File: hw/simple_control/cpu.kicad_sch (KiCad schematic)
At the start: 12 parts, among them J601 Conn_01x04, J602 Raspberry_Pi_0_2_3, J603 Conn_01x03, SW601 SW_Push, U601 PicoW

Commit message: chore(hw): assign footprints
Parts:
- C601, C602, C603: footprint (none) -> Capacitor_SMD:C_0805_2012Metric_Pad1.18x1.45mm_HandSolder
- J602: footprint (none) -> my:Raspberry_Pi_Zero_Socketed_THT_FaceDown_MountingHoles_No_Courtyard
- J603: footprint (none) -> Connector_PinHeader_2.54mm:PinHeader_1x03_P2.54mm_Vertical
- JP601, JP602: footprint (none) -> Jumper:SolderJumper-3_P1.3mm_Bridged12_RoundedPad1.0x1.5mm_NumberLabels
- SW601: footprint (none) -> Button_Switch_THT:SW_PUSH_6mm
- U601: footprint RPi_PicoW:RPi_Pico_SMD_TH -> rp-pico:RPi_PicoW_SMD_TH
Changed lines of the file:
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@@
       (effects (font (size 1.27 1.27)) (justify left))
     )
-    (property "Footprint" "" (at 162.2552 184.15 0)
+    (property "Footprint" "Capacitor_SMD:C_0805_2012Metric_Pad1.18x1.45mm_HandSolder" (at 162.2552 184.15 0)
       (effects (font (size 1.27 1.27)) hide)
     )
@@
       (effects (font (size 1.27 1.27)) (justify left))
     )
-    (property "Footprint" "" (at 81.28 138.43 0)
+    (property "Footprint" "Connector_PinHeader_2.54mm:PinHeader_1x03_P2.54mm_Vertical" (at 81.28 138.43 0)
       (effects (font (size 1.27 1.27)) hide)
     )
@@
   (symbol (lib_id "power:GND") (at 135.89 187.96 0) (unit 1)
     (in_bom yes) (on_board yes) (dnp no) (fields_autoplaced)
-    (property "Reference" "#PWR0618" (at 135.89 194.31 0)
+    (property "Reference" "#PWR0619" (at 135.89 194.31 0)
       (effects (font (size 1.27 1.27)) hide)
     )
@@
       (project "simple_control"
         (path "/063164e8-0d2a-492b-8a61-e4fa4fbf06a6/3d4e7106-28aa-4335-9fa1-cc7761972854"
-          (reference "#PWR0618") (unit 1)
+          (reference "#PWR0619") (unit 1)
         )
       )
@@
       (effects (font (size 1.27 1.27)) (justify left))
     )
-    (property "Footprint" "" (at 136.8552 184.15 0)
+    (property "Footprint" "Capacitor_SMD:C_0805_2012Metric_Pad1.18x1.45mm_HandSolder" (at 136.8552 184.15 0)
       (effects (font (size 1.27 1.27)) hide)
     )
@@
       (effects (font (size 1.27 1.27)))
     )
-    (property "Footprint" "" (at 259.08 154.94 0)
+    (property "Footprint" "Jumper:SolderJumper-3_P1.3mm_Bridged12_RoundedPad1.0x1.5mm_NumberLabels" (at 259.08 154.94 0)
       (effects (font (size 1.27 1.27)) hide)
     )
@@
       (effects (font (size 1.27 1.27)))
     )
-    (property "Footprint" "" (at 259.08 142.24 0)
+    (property "Footprint" "Jumper:SolderJumper-3_P1.3mm_Bridged12_RoundedPad1.0x1.5mm_NumberLabels" (at 259.08 142.24 0)
       (effects (font (size 1.27 1.27)) hide)
     )
@@
       (effects (font (size 1.27 1.27)) (justify left))
     )
-    (property "Footprint" "" (at 149.5552 184.15 0)
+    (property "Footprint" "Capacitor_SMD:C_0805_2012Metric_Pad1.18x1.45mm_HandSolder" (at 149.5552 184.15 0)
       (effects (font (size 1.27 1.27)) hide)
     )
@@
   (symbol (lib_id "power:GND") (at 88.9 132.08 0) (unit 1)
     (in_bom yes) (on_board yes) (dnp no) (fields_autoplaced)
-    (property "Reference" "#PWR0619" (at 88.9 138.43 0)
+    (property "Reference" "#PWR0617" (at 88.9 138.43 0)
       (effects (font (size 1.27 1.27)) hide)
     )
@@
       (project "simple_control"
         (path "/063164e8-0d2a-492b-8a61-e4fa4fbf06a6/3d4e7106-28aa-4335-9fa1-cc7761972854"
-          (reference "#PWR0619") (unit 1)
+          (reference "#PWR0617") (unit 1)
         )
       )
@@
   (symbol (lib_id "power:+5V") (at 135.89 172.72 0) (unit 1)
     (in_bom yes) (on_board yes) (dnp no) (fields_autoplaced)
-    (property "Reference" "#PWR0617" (at 135.89 176.53 0)
+    (property "Reference" "#PWR0618" (at 135.89 176.53 0)
       (effects (font (size 1.27 1.27)) hide)
     )
@@
       (project "simple_control"
         (path "/063164e8-0d2a-492b-8a61-e4fa4fbf06a6/3d4e7106-28aa-4335-9fa1-cc7761972854"
-          (reference "#PWR0617") (unit 1)
+          (reference "#PWR0618") (unit 1)
         )
       )
@@
       (effects (font (size 1.27 1.27)))
     )
-    (property "Footprint" "RPi_PicoW:RPi_Pico_SMD_TH" (at 81.28 99.06 90)
+    (property "Footprint" "rp-pico:RPi_PicoW_SMD_TH" (at 81.28 99.06 90)
       (effects (font (size 1.27 1.27)) hide)
     )
@@
       (effects (font (size 1.27 1.27)) (justify left))
     )
-    (property "Footprint" "" (at 165.1 102.87 0)
+    (property "Footprint" "Button_Switch_THT:SW_PUSH_6mm" (at 165.1 102.87 0)
       (effects (font (size 1.27 1.27)) hide)
     )
@@
       (effects (font (size 1.27 1.27)) (justify left))
     )
-    (property "Footprint" "" (at 218.44 62.23 0)
-      (effects (font (size 1.27 1.27)) hide)
-    )
+    (property "Footprint" "my:Raspberry_Pi_Zero_Socketed_THT_FaceDown_MountingHoles_No_Courtyard" (at 218.44 62.23 0)
+      (effects (font (size 1.27 1.27)) hide)
+    )

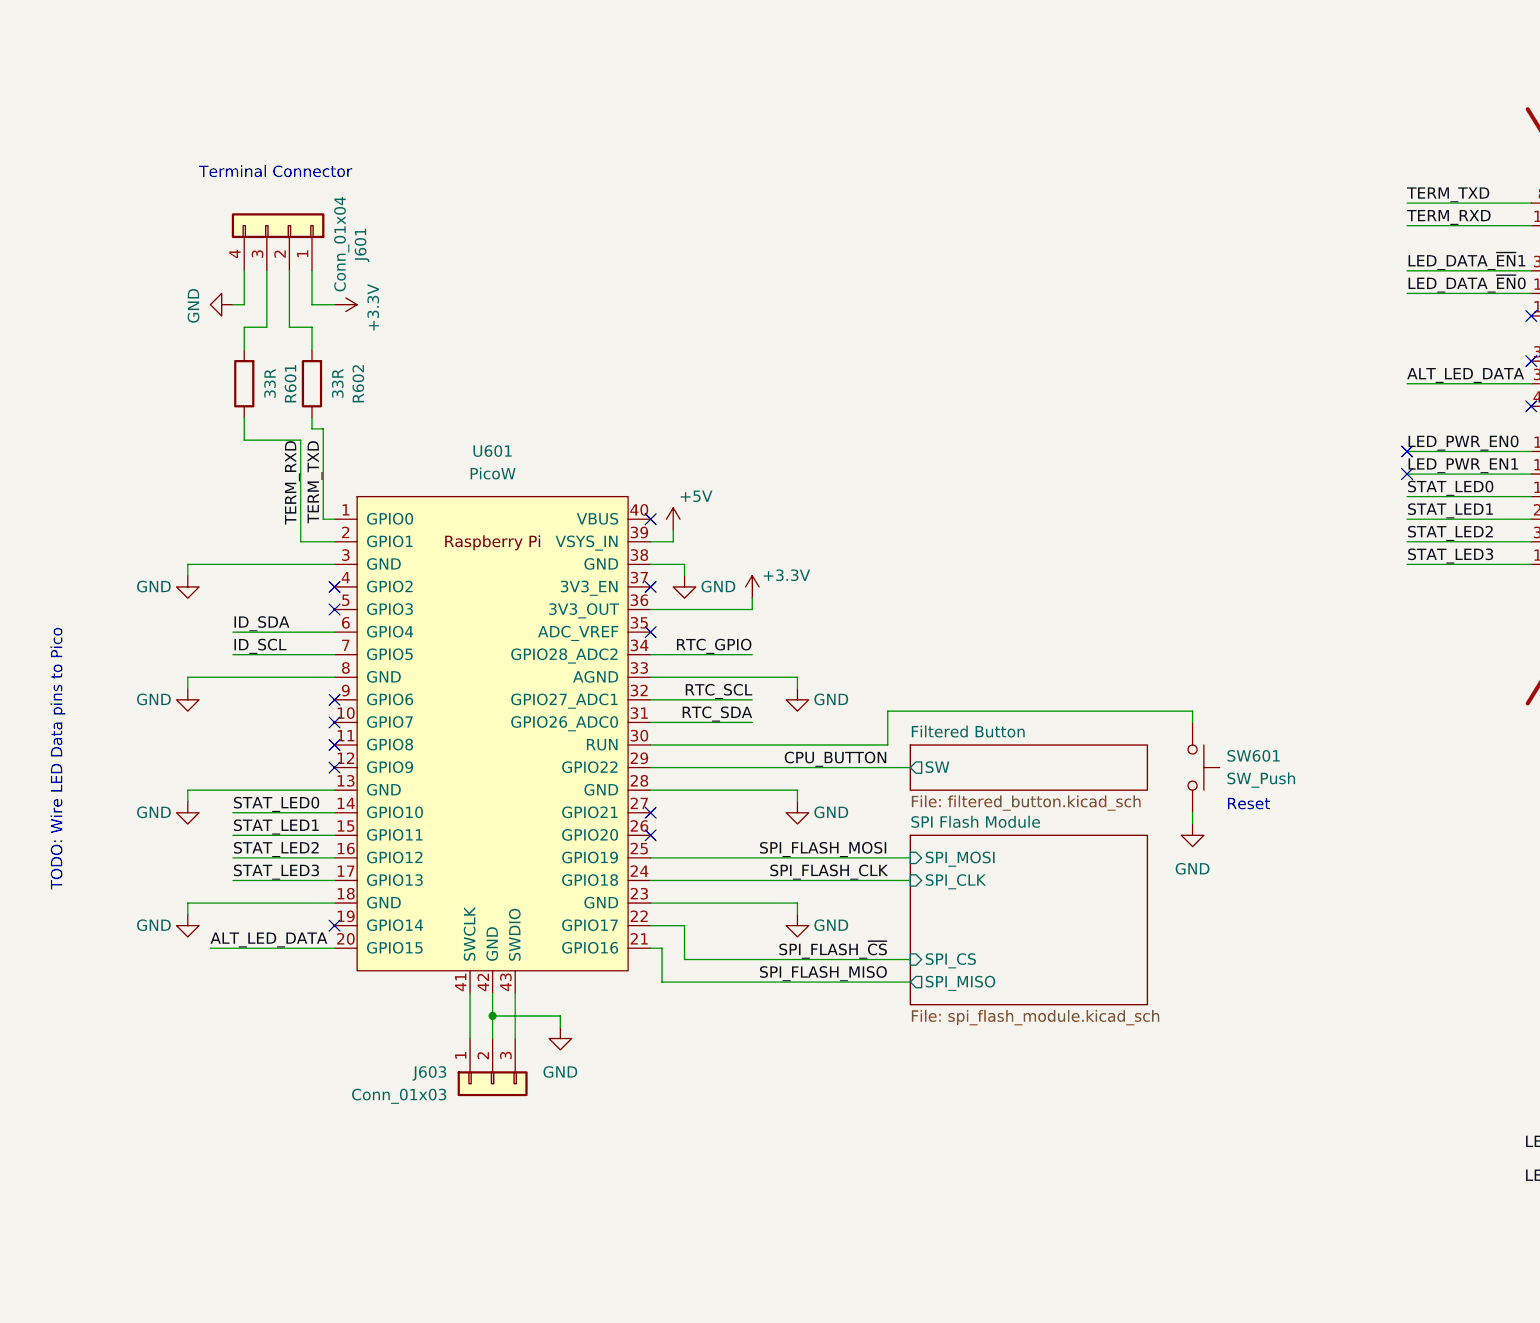
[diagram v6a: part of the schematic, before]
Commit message: chore(hw): wire LEDs to Pico, other improvements
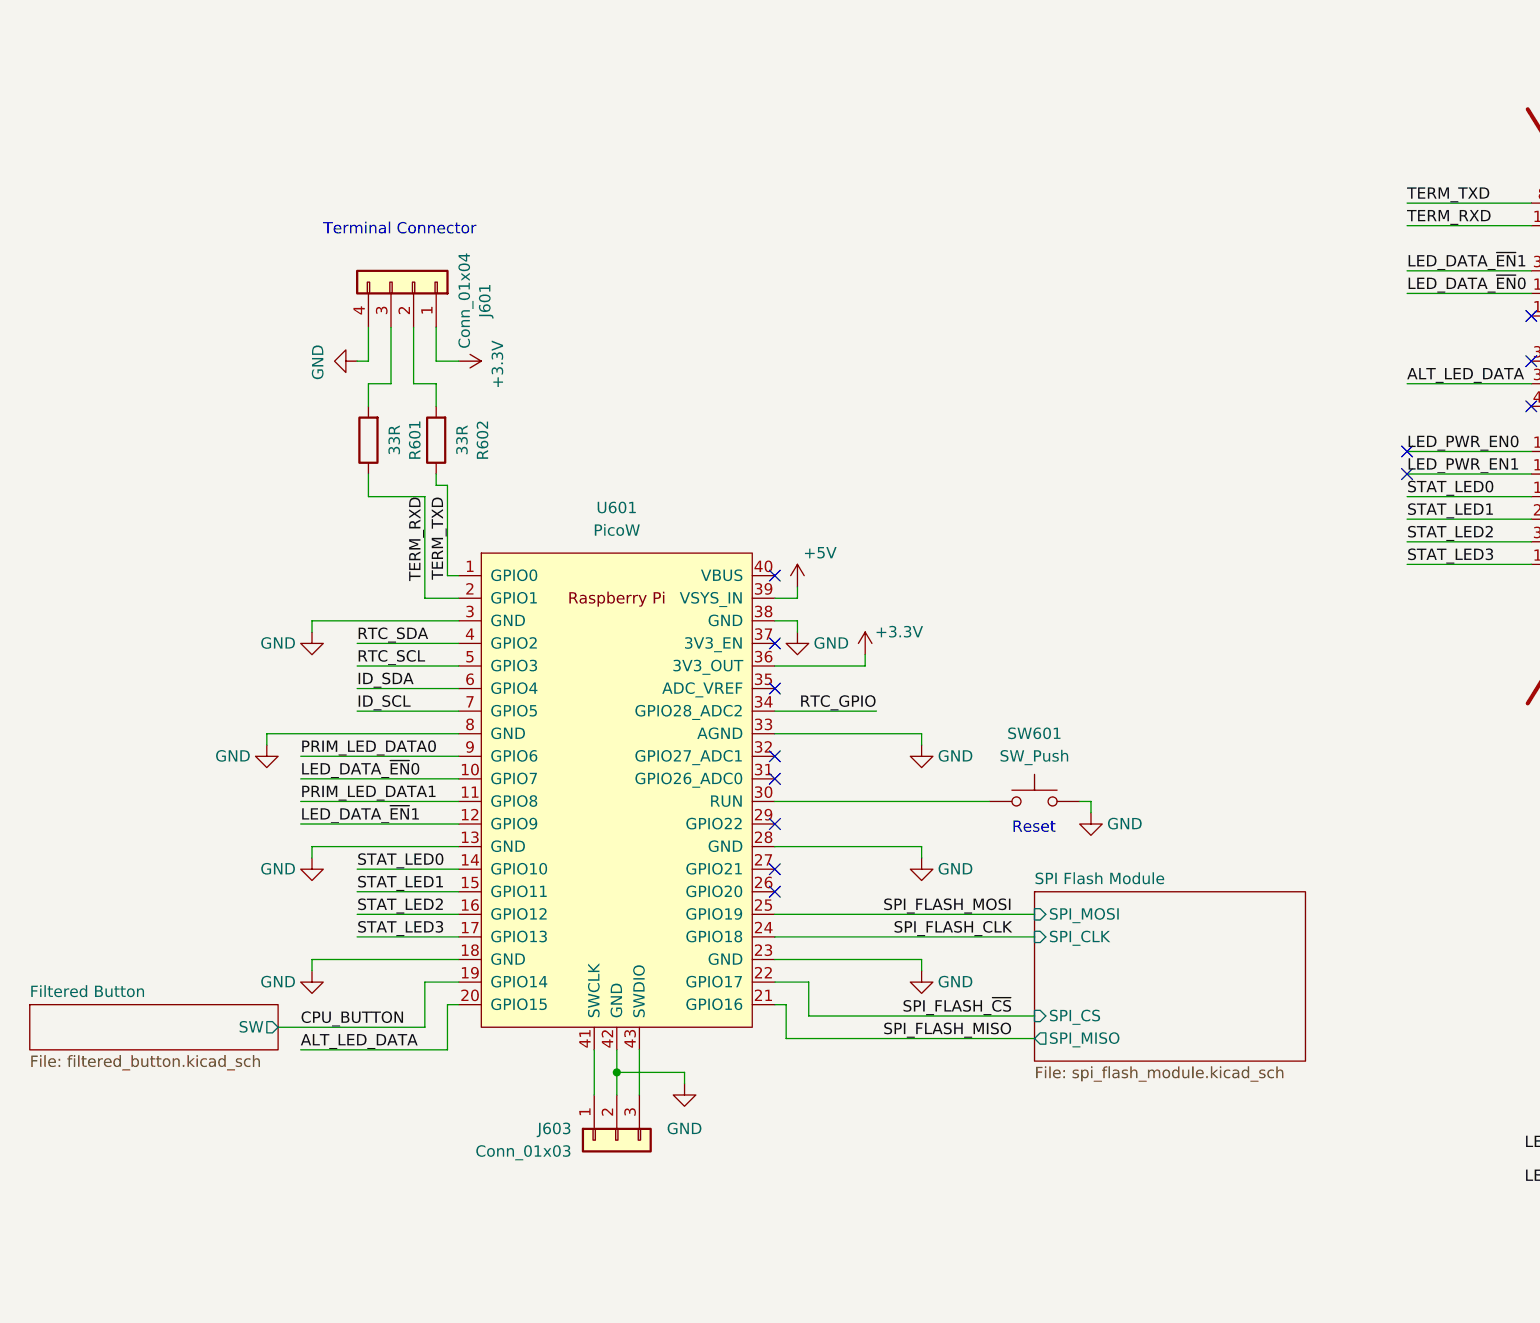
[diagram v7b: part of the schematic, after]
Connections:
- net CPU_BUTTON: now also U601.19 (GPIO14); no longer U601.29 (GPIO22)
- net LED_DATA_~{EN}0: now also U601.10 (GPIO7)
- net LED_DATA_~{EN}1: now also U601.12 (GPIO9)
- net PRIM_LED_DATA0: now also U601.9 (GPIO6)
- net PRIM_LED_DATA1: now also U601.11 (GPIO8)
- net RTC_SCL: now also U601.5 (GPIO3); no longer U601.32 (GPIO27_ADC1)
- net RTC_SDA: now also U601.4 (GPIO2); no longer U601.31 (GPIO26_ADC0)
- no-connect marks 19 -> 15
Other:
- note removed: "TODO: Wire LED Data pins to Pico"
- moved on the sheet: J601, J603, R601, R602, SW601, U601

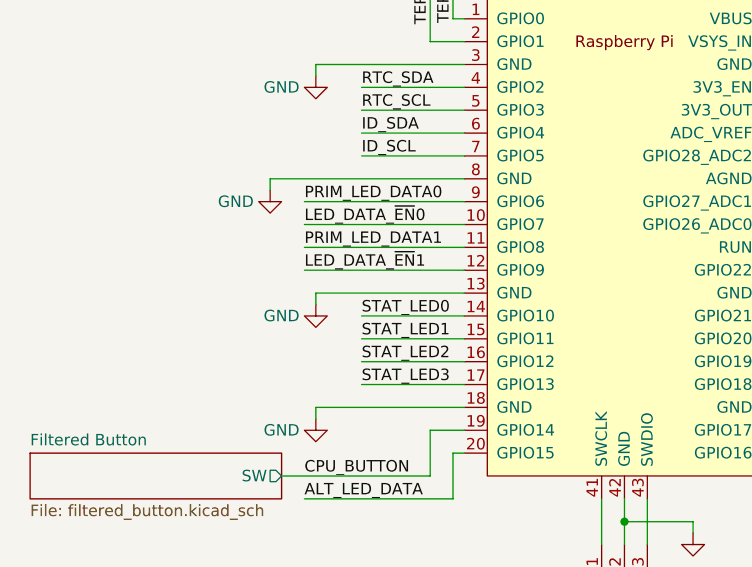
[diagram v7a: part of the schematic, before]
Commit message: chore(hw): layout module interconnects
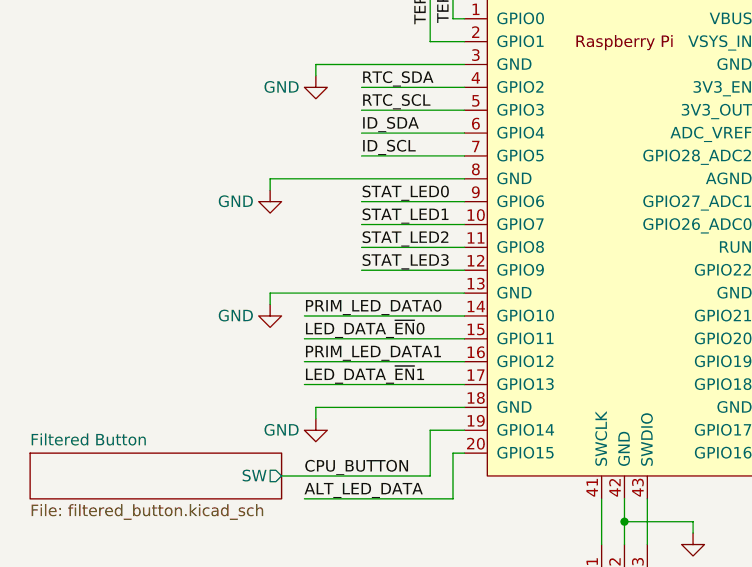
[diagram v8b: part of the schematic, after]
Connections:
- net LED_DATA_~{EN}0: now also U601.15 (GPIO11); no longer U601.10 (GPIO7)
- net LED_DATA_~{EN}1: now also U601.17 (GPIO13); no longer U601.12 (GPIO9)
- net PRIM_LED_DATA0: now also U601.14 (GPIO10); no longer U601.9 (GPIO6)
- net PRIM_LED_DATA1: now also U601.16 (GPIO12); no longer U601.11 (GPIO8)
- net STAT_LED0: now also U601.9 (GPIO6); no longer U601.14 (GPIO10)
- net STAT_LED1: now also U601.10 (GPIO7); no longer U601.15 (GPIO11)
- net STAT_LED2: now also U601.11 (GPIO8); no longer U601.16 (GPIO12)
- net STAT_LED3: now also U601.12 (GPIO9); no longer U601.17 (GPIO13)
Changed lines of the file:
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@@
     (stroke (width 0) (type default))
   )
-  (wire (pts (xy 59.69 101.6) (xy 77.47 101.6))
+  (wire (pts (xy 59.69 114.3) (xy 77.47 114.3))
     (stroke (width 0) (type default))
   )
@@
     (stroke (width 0) (type default))
   )
-  (wire (pts (xy 60.96 113.03) (xy 60.96 111.76))
+  (wire (pts (xy 55.88 113.03) (xy 55.88 111.76))
     (stroke (width 0) (type default))
   )
@@
     (stroke (width 0) (type default))
   )
-  (wire (pts (xy 66.04 121.92) (xy 77.47 121.92))
+  (wire (pts (xy 66.04 109.22) (xy 77.47 109.22))
     (stroke (width 0) (type default))
   )
@@
     (stroke (width 0) (type default))
   )
-  (wire (pts (xy 60.96 111.76) (xy 77.47 111.76))
+  (wire (pts (xy 55.88 111.76) (xy 77.47 111.76))
     (stroke (width 0) (type default))
   )
@@
     (stroke (width 0) (type default))
   )
-  (wire (pts (xy 66.04 119.38) (xy 77.47 119.38))
+  (wire (pts (xy 66.04 106.68) (xy 77.47 106.68))
     (stroke (width 0) (type default))
   )
@@
     (stroke (width 0) (type default))
   )
-  (wire (pts (xy 59.69 104.14) (xy 77.47 104.14))
+  (wire (pts (xy 59.69 116.84) (xy 77.47 116.84))
     (stroke (width 0) (type default))
   )
@@
     (stroke (width 0) (type default))
   )
-  (wire (pts (xy 59.69 109.22) (xy 77.47 109.22))
+  (wire (pts (xy 59.69 121.92) (xy 77.47 121.92))
     (stroke (width 0) (type default))
   )
@@
     (stroke (width 0) (type default))
   )
-  (wire (pts (xy 66.04 116.84) (xy 77.47 116.84))
+  (wire (pts (xy 66.04 104.14) (xy 77.47 104.14))
     (stroke (width 0) (type default))
   )
@@
     (stroke (width 0) (type default))
   )
-  (wire (pts (xy 59.69 106.68) (xy 77.47 106.68))
+  (wire (pts (xy 59.69 119.38) (xy 77.47 119.38))
     (stroke (width 0) (type default))
   )
@@
     (stroke (width 0) (type default))
   )
-  (wire (pts (xy 66.04 114.3) (xy 77.47 114.3))
+  (wire (pts (xy 66.04 101.6) (xy 77.47 101.6))
     (stroke (width 0) (type default))
   )
@@
     (effects (font (size 1.27 1.27)) (justify left bottom))
   )
-  (label "STAT_LED3" (at 66.04 121.92 0) (fields_autoplaced)
+  (label "STAT_LED3" (at 66.04 109.22 0) (fields_autoplaced)
     (effects (font (size 1.27 1.27)) (justify left bottom))
   )
@@
     (effects (font (size 1.27 1.27)) (justify right bottom))
   )
-  (label "STAT_LED1" (at 66.04 116.84 0) (fields_autoplaced)
+  (label "STAT_LED1" (at 66.04 104.14 0) (fields_autoplaced)
     (effects (font (size 1.27 1.27)) (justify left bottom))
   )
@@
     (effects (font (size 1.27 1.27)) (justify right bottom))
   )
-  (label "STAT_LED2" (at 66.04 119.38 0) (fields_autoplaced)
+  (label "STAT_LED2" (at 66.04 106.68 0) (fields_autoplaced)
     (effects (font (size 1.27 1.27)) (justify left bottom))
   )
@@
     (effects (font (size 1.27 1.27)) (justify left bottom))
   )
-  (label "PRIM_LED_DATA0" (at 59.69 101.6 0) (fields_autoplaced)
+  (label "PRIM_LED_DATA0" (at 59.69 114.3 0) (fields_autoplaced)
     (effects (font (size 1.27 1.27)) (justify left bottom))
   )
@@
     (effects (font (size 1.27 1.27)) (justify right bottom))
   )
-  (label "LED_DATA_~{EN}1" (at 59.69 109.22 0) (fields_autoplaced)
-    (effects (font (size 1.27 1.27)) (justify left bottom))
-  )
-  (label "STAT_LED0" (at 66.04 114.3 0) (fields_autoplaced)
-    (effects (font (size 1.27 1.27)) (justify left bottom))
-  )
-  (label "PRIM_LED_DATA1" (at 59.69 106.68 0) (fields_autoplaced)
+  (label "LED_DATA_~{EN}1" (at 59.69 121.92 0) (fields_autoplaced)
+    (effects (font (size 1.27 1.27)) (justify left bottom))
+  )
+  (label "STAT_LED0" (at 66.04 101.6 0) (fields_autoplaced)
+    (effects (font (size 1.27 1.27)) (justify left bottom))
+  )
+  (label "PRIM_LED_DATA1" (at 59.69 119.38 0) (fields_autoplaced)
     (effects (font (size 1.27 1.27)) (justify left bottom))
   )
@@
     (effects (font (size 1.27 1.27)) (justify left bottom))
   )
-  (label "LED_DATA_~{EN}0" (at 59.69 104.14 0) (fields_autoplaced)
+  (label "LED_DATA_~{EN}0" (at 59.69 116.84 0) (fields_autoplaced)
     (effects (font (size 1.27 1.27)) (justify left bottom))
   )
@@
     )
   )
-  (symbol (lib_id "power:GND") (at 60.96 113.03 0) (unit 1)
-    (in_bom yes) (on_board yes) (dnp no)
-    (property "Reference" "#PWR0612" (at 60.96 119.38 0)
-      (effects (font (size 1.27 1.27)) hide)
-    )
-    (property "Value" "GND" (at 57.15 114.3 0)
-      (effects (font (size 1.27 1.27)))
-    )
-    (property "Footprint" "" (at 60.96 113.03 0)
-      (effects (font (size 1.27 1.27)) hide)
-    )
-    (property "Datasheet" "" (at 60.96 113.03 0)
-      (effects (font (size 1.27 1.27)) hide)
-    )
+  (symbol (lib_id "power:GND") (at 55.88 113.03 0) (unit 1)
+    (in_bom yes) (on_board yes) (dnp no)
+    (property "Reference" "#PWR0612" (at 55.88 119.38 0)
+      (effects (font (size 1.27 1.27)) hide)
+    )
+    (property "Value" "GND" (at 52.07 114.3 0)
+      (effects (font (size 1.27 1.27)))
+    )
+    (property "Footprint" "" (at 55.88 113.03 0)
+      (effects (font (size 1.27 1.27)) hide)
+    )
+    (property "Datasheet" "" (at 55.88 113.03 0)
+      (effects (font (size 1.27 1.27)) hide)
+    )
